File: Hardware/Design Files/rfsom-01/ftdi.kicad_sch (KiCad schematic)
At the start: 26 parts

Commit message: some ddr routing progress; layerstack per pcbway standard options, review reqd; commit prior to ddr split;
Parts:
- C33, C36, C38, C39, C40: renamed from C?; footprint Capacitor_SMD:C_0805_2012Metric_Pad1.18x1.45mm_HandSolder -> Capacitor_SMD:C_0805_2012Metric
- C35, C41, C42, C43, C44, C45: renamed from C?; footprint Capacitor_SMD:C_0402_1005Metric_Pad0.74x0.62mm_HandSolder -> Capacitor_SMD:C_0402_1005Metric
- D1, D2: renamed from D?; footprint LED_SMD:LED_0603_1608Metric_Pad1.05x0.95mm_HandSolder -> LED_SMD:LED_0603_1608Metric
- R36, R37, R38, R39, R40, R41: renamed from R?; footprint Resistor_SMD:R_0603_1608Metric_Pad0.98x0.95mm_HandSolder -> Resistor_SMD:R_0603_1608Metric
- gave numbers to parts that had none: 7

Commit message: added starage, usb sch; more design progress in sch;
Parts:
- added C199: CL21B475KAFNNNE, Capacitor_SMD:C_0805_2012Metric_Pad1.18x1.45mm_HandSolder, symbol Capacitors:CL21B475KAFNNNE
- added C200: CL10B105KA8NNNC, Capacitor_SMD:C_0603_1608Metric_Pad1.08x0.95mm_HandSolder, symbol Capacitors:CL10B105KA8NNNC
- added C201: CL05B104KA5NNNC, Capacitor_SMD:C_0402_1005Metric, symbol Capacitors:CL05B104KA5NNNC
- added FB1, FB12: MPZ1608S601ATA00, Resistor_SMD:R_0603_1608Metric, symbol Inductors:MPZ1608S601ATA00
- added J2: 1054550101, Connectors:1054550101, symbol Connectors:1054550101
- added R137, R139, R140: RC0603FR-0710KL, Resistor_SMD:R_0603_1608Metric, symbol Resistors:RC0603FR-0710KL
- added R138: RC0603FR-072KL, Resistor_SMD:R_0603_1608Metric_Pad0.98x0.95mm_HandSolder, symbol Resistors:RC0603FR-072KL
- added R6, R7: RC0603FR-135K11L, Resistor_SMD:R_0603_1608Metric, symbol Resistors:RC0603FR-135K11L
- added U16: 93LC56BT-I/OT, Package_TO_SOT_SMD:SOT-23-6, symbol ICs:93LC56BT-I/OT
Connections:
- net +VCC_3V3: now also C201.1, R137.1, R139.1, R140.1, U16.6 (VCC)
- net +VIN_5V0: now also FB1.2
- net FTDI_USB_D+: now also U4.6 (DM), J2.A6 (D1+), J2.B6 (D2+); no longer U4.7 (DP)
- net FTDI_USB_D-: now also U4.7 (DP), J2.A7 (D1-), J2.B7 (D2-); no longer U4.6 (DM)
- net GND: now also C201.2, FB12.2, U16.2 (VSS)
- net FTDI_EEDATA: now reaches U4.43 (EEDATA)
- net FTDI_EEDATA: now also R138.2, R140.2, U16.3 (DI)
- net FTDI_EECLK: now reaches U4.44 (EECLK)
- net FTDI_EECLK: now also R139.2, U16.4 (CLK)
- net FTDI_EECS: now reaches U4.45 (EECS)
- net FTDI_EECS: now also R137.2, U16.5 (CS)
- new net: J2.A5 (CC1), R6.1
- new net: J2.B5 (CC2), R7.1
- new net: R138.1, U16.1 (DO)
- new net +VUSB: C199.1, C200.1, FB1.1, J2.A4 (VBUS), J2.A9 (VBUS), J2.B4 (VBUS), J2.B9 (VBUS)
- new net GND_USB: C199.2, C200.2, FB12.1, J2.A1 (GND), J2.A12 (GND), J2.B1 (GND), J2.B12 (GND), J2.SH1 (SHIELD1), J2.SH2 (SHIELD2), R6.2, R7.2
- new net USBC_RX1-N: J2.B10 (RX1-)
- new net USBC_RX1-P: J2.B11 (RX1+)
- new net USBC_RX2-N: J2.A10 (RX2-)
- new net USBC_RX2-P: J2.A11 (RX2+)
- new net USBC_TX1-N: J2.A3 (TX1-)
- new net USBC_TX1-P: J2.A2 (TX1+)
- new net USBC_TX2-N: J2.B3 (TX2-)
- new net USBC_TX2-P: J2.B2 (TX2+)
- no-connect marks 0 -> 8
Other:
- note added: "!"
- moved on the sheet: C33, C34, C35, C36, C37, C38, C39, C40, C41, C42, C43, C44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

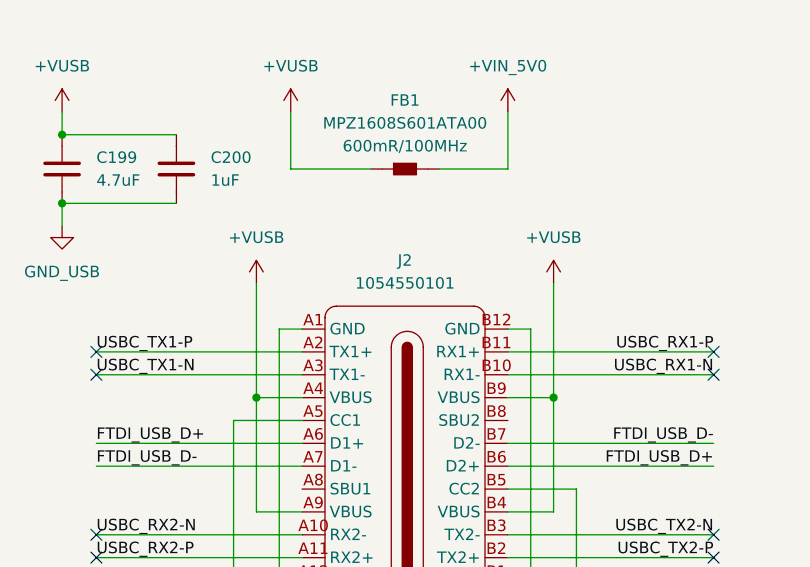
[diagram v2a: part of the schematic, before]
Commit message: routing changes; added mezzanine; added pl ram;
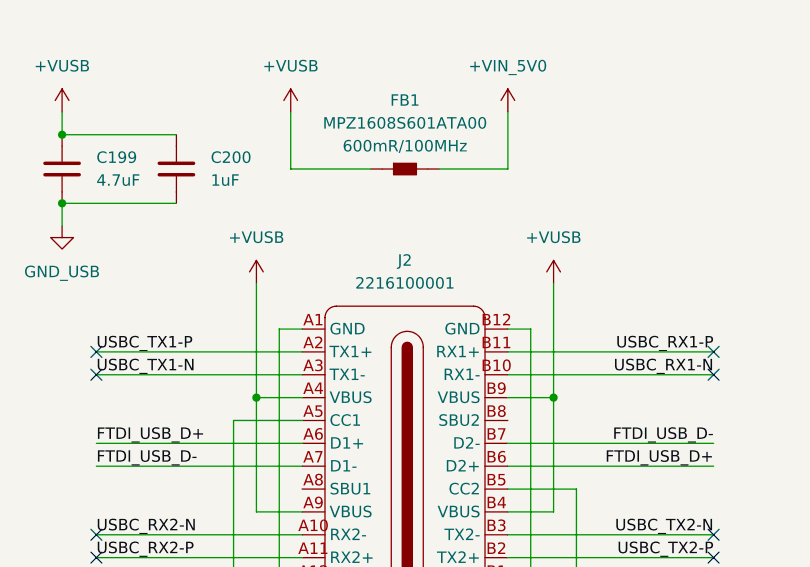
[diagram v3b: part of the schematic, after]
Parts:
- removed J2: 1054550101, Connectors:1054550101, symbol Connectors:1054550101
- added J2: 2216100001, Connectors:2216100001, symbol Connectors:2216100001
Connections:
- net +VUSB: now also J2.A4 (VBUS), J2.A9 (VBUS), J2.B4 (VBUS), J2.B9 (VBUS)
- net FTDI_USB_D+: now also J2.A6 (D1+), J2.B6 (D2+)
- net FTDI_USB_D-: now also J2.A7 (D1-), J2.B7 (D2-)
- net GND_USB: now also J2.A1 (GND), J2.A12 (GND), J2.B1 (GND), J2.B12 (GND), J2.SH1 (SHIELD1), J2.SH2 (SHIELD2)
- net USBC_RX1-N: now also J2.B10 (RX1-)
- net USBC_RX1-P: now also J2.B11 (RX1+)
- net USBC_RX2-N: now also J2.A10 (RX2-)
- net USBC_RX2-P: now also J2.A11 (RX2+)
- net USBC_TX1-N: now also J2.A3 (TX1-)
- net USBC_TX1-P: now also J2.A2 (TX1+)
- net USBC_TX2-N: now also J2.B3 (TX2-)
- net USBC_TX2-P: now also J2.B2 (TX2+)
- net at R6.1: now also J2.A5 (CC1)
- net at R7.1: now also J2.B5 (CC2)

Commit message: replaced pmic;
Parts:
- C199: footprint Capacitor_SMD:C_0805_2012Metric_Pad1.18x1.45mm_HandSolder -> Capacitor_SMD:C_0805_2012Metric
- C200: footprint Capacitor_SMD:C_0603_1608Metric_Pad1.08x0.95mm_HandSolder -> Capacitor_SMD:C_0603_1608Metric
- R138: footprint Resistor_SMD:R_0603_1608Metric_Pad0.98x0.95mm_HandSolder -> Resistor_SMD:R_0603_1608Metric
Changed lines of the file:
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@@
 			)
 		)
-		(property "Footprint" "Capacitor_SMD:C_0805_2012Metric_Pad1.18x1.45mm_HandSolder"
+		(property "Footprint" "Capacitor_SMD:C_0805_2012Metric"
 			(at 20.32 29.21 0)
 			(effects
@@
 			)
 		)
-		(property "Footprint" "Capacitor_SMD:C_0603_1608Metric_Pad1.08x0.95mm_HandSolder"
+		(property "Footprint" "Capacitor_SMD:C_0603_1608Metric"
 			(at 33.02 29.21 0)
 			(effects
@@
 			)
 		)
-		(property "Footprint" "Resistor_SMD:R_0603_1608Metric_Pad0.98x0.95mm_HandSolder"
+		(property "Footprint" "Resistor_SMD:R_0603_1608Metric"
 			(at 67.31 153.67 0)
 			(effects
